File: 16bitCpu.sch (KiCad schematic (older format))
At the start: 0 parts

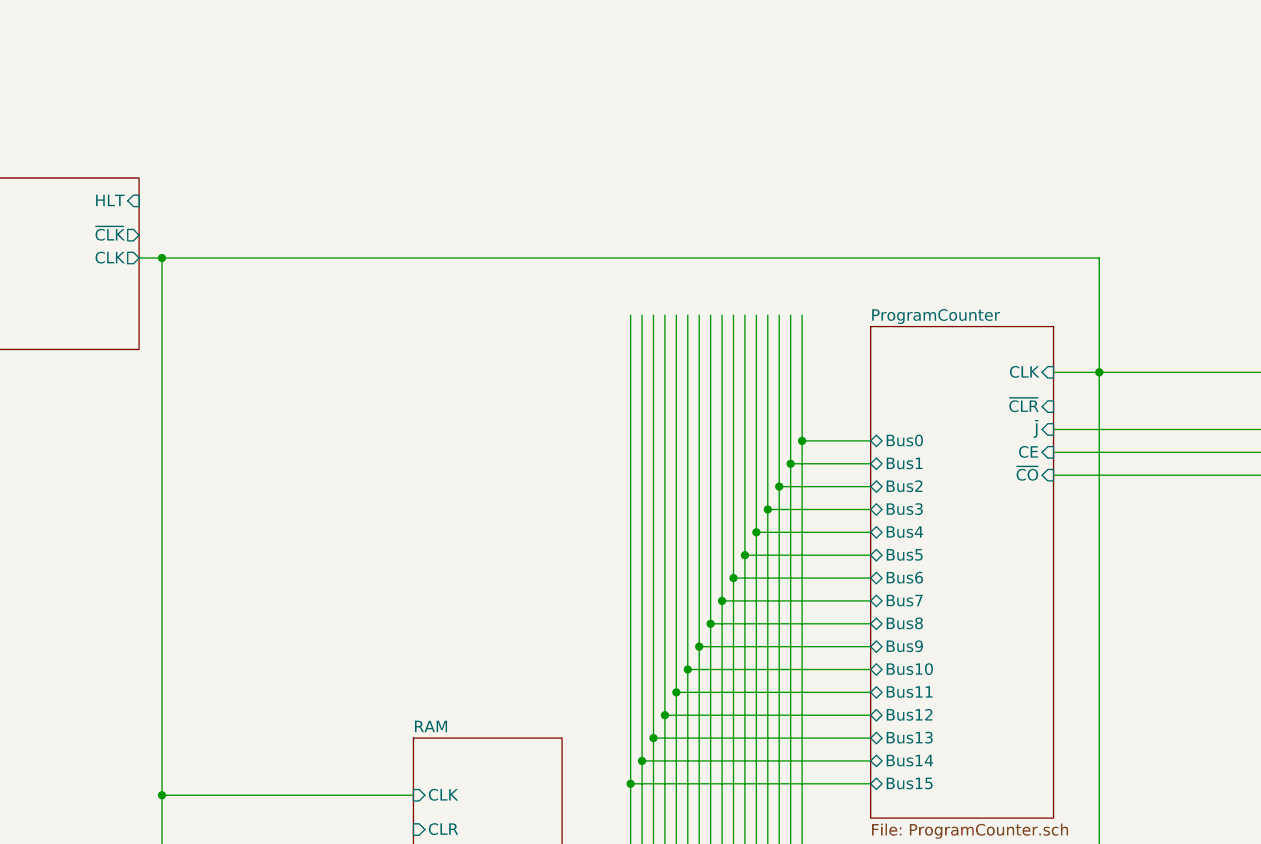
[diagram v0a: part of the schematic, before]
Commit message: changed ir to only hold 12
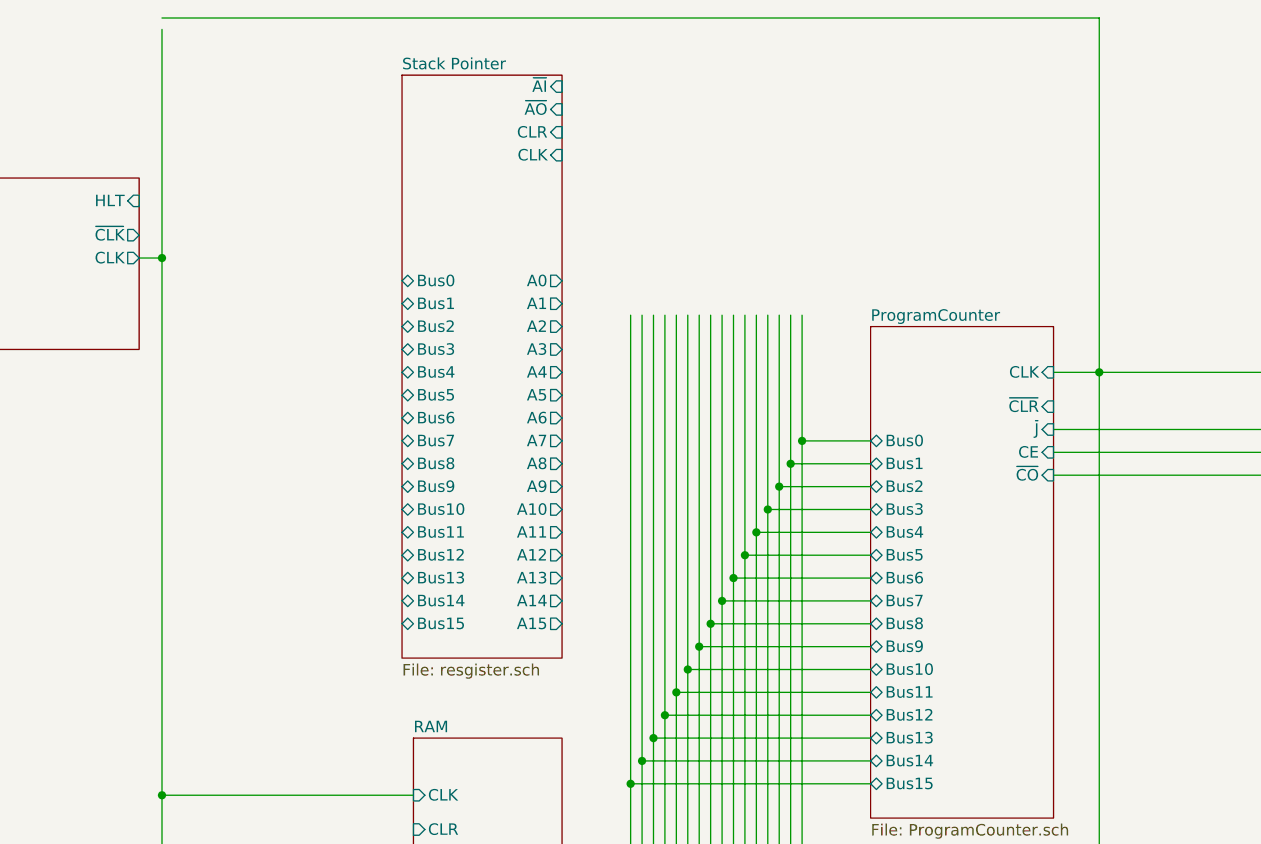
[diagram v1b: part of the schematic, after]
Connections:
- wire segments 411 -> 412
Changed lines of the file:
@@
 	7200 2100 7400 2100
-Wire Wire Line
-	7400 2100 7400 1600
 Wire Wire Line
 	5000 7250 6100 7250
@@
 F23 "~MEMWE" I L 4400 4850 50
 $EndSheet
-Connection ~ 3300 1600
 $Sheet
 S 4350 7100 650  1900
@@
 Connection ~ 7400 2100
 Wire Wire Line
-	3300 1600 7400 1600
+	3300 550  7400 550
 Wire Wire Line
 	7100 7800 7200 7800
@@
 Wire Wire Line
 	2650 7450 2650 13800
+$Sheet
+S 4350 800  700  2550
+U 5FB94562
+F0 "Stack Pointer" 50
+F1 "resgister.sch" 50
+F2 "CLK" I R 5050 1150 50
+F3 "Bus0" T L 4350 1700 50
+F4 "CLR" I R 5050 1050 50
+F5 "Bus1" T L 4350 1800 50
+F6 "Bus2" T L 4350 1900 50
+F7 "Bus3" T L 4350 2000 50
+F8 "Bus4" T L 4350 2100 50
+F9 "Bus5" T L 4350 2200 50
+F10 "Bus6" T L 4350 2300 50
+F11 "Bus7" T L 4350 2400 50
+F12 "Bus8" T L 4350 2500 50
+F13 "Bus9" T L 4350 2600 50
+F14 "Bus10" T L 4350 2700 50
+F15 "Bus11" T L 4350 2800 50
+F16 "Bus12" T L 4350 2900 50
+F17 "Bus13" T L 4350 3000 50
+F18 "Bus14" T L 4350 3100 50
+F19 "Bus15" T L 4350 3200 50
+F20 "A0" O R 5050 1700 50
+F21 "A1" O R 5050 1800 50
+F22 "A2" O R 5050 1900 50
+F23 "A3" O R 5050 2000 50
+F24 "A4" O R 5050 2100 50
+F25 "A5" O R 5050 2200 50
+F26 "A6" O R 5050 2300 50
+F27 "A7" O R 5050 2400 50
+F28 "A8" O R 5050 2500 50
+F29 "A9" O R 5050 2600 50
+F30 "A10" O R 5050 2700 50
+F31 "A11" O R 5050 2800 50
+F32 "A12" O R 5050 2900 50
+F33 "A13" O R 5050 3000 50
+F34 "A14" O R 5050 3100 50
+F35 "A15" O R 5050 3200 50
+F36 "~AO" I R 5050 950 50
+F37 "~AI" I R 5050 850 50
+$EndSheet
+Wire Wire Line
+	7400 550  7400 2100
+Wire Wire Line
+	3300 600  3300 1600
+Connection ~ 3300 1600
 $EndSCHEMATC

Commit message: non floating ram and ir , added stack register
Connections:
- wire segments 412 -> 452
- no-connect marks 0 -> 31
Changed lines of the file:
@@
 $Descr A3 11693 16535 portrait
 encoding utf-8
-Sheet 1 9
+Sheet 1 10
 Title ""
 Date ""
@@
 $EndDescr
 Wire Wire Line
-	5400 1850 5400 3800
-Wire Wire Line
-	5500 1850 5500 3600
-Wire Wire Line
-	5550 1850 5550 3500
-Wire Wire Line
-	5600 1850 5600 3400
-Wire Wire Line
-	5650 1850 5650 3300
-Wire Wire Line
-	5700 1850 5700 3200
-Wire Wire Line
-	5750 1850 5750 3100
-Wire Wire Line
-	5850 1850 5850 2900
-Wire Wire Line
-	5900 1850 5900 2800
-Wire Wire Line
-	5950 1850 5950 2700
-Wire Wire Line
-	6000 1850 6000 2600
-Wire Wire Line
-	6050 1850 6050 2500
+	5400 1850 5400 3200
+Wire Wire Line
+	5500 1850 5500 3000
+Wire Wire Line
+	5550 1850 5550 2900
+Wire Wire Line
+	5600 1850 5600 2800
+Wire Wire Line
+	5650 1850 5650 2700
+Wire Wire Line
+	5700 1850 5700 2600
+Wire Wire Line
+	5750 1850 5750 2500
+Wire Wire Line
+	5850 1850 5850 2300
+Wire Wire Line
+	5900 1850 5900 2200
+Wire Wire Line
+	5950 1850 5950 2100
+Wire Wire Line
+	6000 1850 6000 2000
+Wire Wire Line
+	6050 1850 6050 1900
 Wire Wire Line
 	6100 5550 6400 5550
@@
 F4 "CLK" O R 3200 1600 50
 $EndSheet
-Wire Wire Line
-	6100 1850 6100 2400
 Connection ~ 6100 4300
 Wire Wire Line
@@
 Connection ~ 5850 4800
 Wire Wire Line
-	5800 1850 5800 3000
+	5800 1850 5800 2400
 Connection ~ 5800 4900
 Wire Wire Line
@@
 	5050 5600 5450 5600
 Wire Wire Line
-	5450 1850 5450 3700
+	5450 1850 5450 3100
 Connection ~ 5450 5600
 Wire Wire Line
@@
 Connection ~ 5350 3900
 Wire Wire Line
-	5350 3900 5350 1850
+	5350 3900 5350 3300
 Wire Wire Line
 	7200 2100 7400 2100
@@
 F30 "CLR" O R 5150 13850 50
 F31 "~CLR" O R 5150 14000 50
+F32 "~SI" O L 4350 13950 50
+F33 "~SO" O L 4350 14050 50
 $EndSheet
 Wire Wire Line
@@
 Wire Wire Line
 	2650 7450 2650 13800
+Wire Wire Line
+	7400 550  7400 2100
+Wire Wire Line
+	3300 600  3300 1600
+Connection ~ 3300 1600
 $Sheet
-S 4350 800  700  2550
+S 4184 1300 816  2200
 U 5FB94562
 F0 "Stack Pointer" 50
-F1 "resgister.sch" 50
-F2 "CLK" I R 5050 1150 50
-F3 "Bus0" T L 4350 1700 50
-F4 "CLR" I R 5050 1050 50
-F5 "Bus1" T L 4350 1800 50
-F6 "Bus2" T L 4350 1900 50
-F7 "Bus3" T L 4350 2000 50
-F8 "Bus4" T L 4350 2100 50
-F9 "Bus5" T L 4350 2200 50
-F10 "Bus6" T L 4350 2300 50
-F11 "Bus7" T L 4350 2400 50
-F12 "Bus8" T L 4350 2500 50
-F13 "Bus9" T L 4350 2600 50
-F14 "Bus10" T L 4350 2700 50
-F15 "Bus11" T L 4350 2800 50
-F16 "Bus12" T L 4350 2900 50
-F17 "Bus13" T L 4350 3000 50
-F18 "Bus14" T L 4350 3100 50
-F19 "Bus15" T L 4350 3200 50
-F20 "A0" O R 5050 1700 50
-F21 "A1" O R 5050 1800 50
-F22 "A2" O R 5050 1900 50
-F23 "A3" O R 5050 2000 50
-F24 "A4" O R 5050 2100 50
-F25 "A5" O R 5050 2200 50
-F26 "A6" O R 5050 2300 50
-F27 "A7" O R 5050 2400 50
-F28 "A8" O R 5050 2500 50
-F29 "A9" O R 5050 2600 50
-F30 "A10" O R 5050 2700 50
-F31 "A11" O R 5050 2800 50
-F32 "A12" O R 5050 2900 50
-F33 "A13" O R 5050 3000 50
-F34 "A14" O R 5050 3100 50
-F35 "A15" O R 5050 3200 50
-F36 "~AO" I R 5050 950 50
-F37 "~AI" I R 5050 850 50
+F1 "stack.sch" 50
+F2 "CLK" I L 4184 1650 50
+F3 "Bus0" T R 5000 1800 50
+F4 "CLR" I L 4184 1550 50
+F5 "Bus1" T R 5000 1900 50
+F6 "Bus2" T R 5000 2000 50
+F7 "Bus3" T R 5000 2100 50
+F8 "Bus4" T R 5000 2200 50
+F9 "Bus5" T R 5000 2300 50
+F10 "Bus6" T R 5000 2400 50
+F11 "Bus7" T R 5000 2500 50
+F12 "Bus8" T R 5000 2600 50
+F13 "Bus9" T R 5000 2700 50
+F14 "Bus10" T R 5000 2800 50
+F15 "Bus11" T R 5000 2900 50
+F16 "Bus12" T R 5000 3000 50
+F17 "Bus13" T R 5000 3100 50
+F18 "Bus14" T R 5000 3200 50
+F19 "Bus15" T R 5000 3300 50
+F20 "~SI" I L 4184 2100 50
+F21 "~SO" I L 4184 2200 50
 $EndSheet
 Wire Wire Line
-	7400 550  7400 2100
-Wire Wire Line
-	3300 600  3300 1600
-Connection ~ 3300 1600
+	3300 1600 3800 1600
+Wire Wire Line
+	3800 1650 4200 1650
+Wire Wire Line
+	5000 1800 6100 1800
+Wire Wire Line
+	6100 1800 6100 2400
+Wire Wire Line
+	5000 1900 6050 1900
+Connection ~ 6050 1900
+Wire Wire Line
+	6050 1900 6050 2500
+Wire Wire Line
+	5000 2000 6000 2000
+Connection ~ 6000 2000
+Wire Wire Line
+	6000 2000 6000 2600
+Wire Wire Line
+	5000 2100 5950 2100
+Connection ~ 5950 2100
+Wire Wire Line
+	5950 2100 5950 2700
+Wire Wire Line
+	5000 2200 5900 2200
+Connection ~ 5900 2200
+Wire Wire Line
+	5900 2200 5900 2800
+Wire Wire Line
+	5000 2300 5850 2300
+Connection ~ 5850 2300
+Wire Wire Line
+	5850 2300 5850 2900
+Wire Wire Line
+	5000 2400 5800 2400
+Connection ~ 5800 2400
+Wire Wire Line
+	5800 2400 5800 3000
+Wire Wire Line
+	5000 2500 5750 2500
+Connection ~ 5750 2500
+Wire Wire Line
+	5750 2500 5750 3100
+Wire Wire Line
+	5000 2600 5700 2600
+Connection ~ 5700 2600
+Wire Wire Line
+	5700 2600 5700 3200
+Wire Wire Line
+	5000 2700 5650 2700
+Connection ~ 5650 2700
+Wire Wire Line
+	5650 2700 5650 3300
+Wire Wire Line
+	5000 2800 5600 2800
+Connection ~ 5600 2800
+Wire Wire Line
+	5600 2800 5600 3400
+Wire Wire Line
+	5000 2900 5550 2900
+Connection ~ 5550 2900
+Wire Wire Line
+	5550 2900 5550 3500
+Wire Wire Line
+	5000 3000 5500 3000
+Connection ~ 5500 3000
+Wire Wire Line
+	5500 3000 5500 3600
+Wire Wire Line
+	5000 3100 5450 3100
+Connection ~ 5450 3100
+Wire Wire Line
+	5450 3100 5450 3700
+Wire Wire Line
+	5000 3200 5400 3200
+Connection ~ 5400 3200
+Wire Wire Line
+	5400 3200 5400 3800
+Wire Wire Line
+	5000 3300 5350 3300
+Connection ~ 5350 3300
+Wire Wire Line
+	5350 3300 5350 1850
+NoConn ~ 6050 1850
+NoConn ~ 6000 1850
+NoConn ~ 5950 1850
+NoConn ~ 5900 1850
+NoConn ~ 5850 1850
+NoConn ~ 5800 1850
+NoConn ~ 5750 1850
+NoConn ~ 5700 1850
+NoConn ~ 5650 1850
+NoConn ~ 5600 1850
+NoConn ~ 5550 1850
+NoConn ~ 5500 1850
+NoConn ~ 5450 1850
+NoConn ~ 5400 1850
+NoConn ~ 5350 1850
+NoConn ~ 5350 15650
+NoConn ~ 5400 15650
+NoConn ~ 5450 15650
+NoConn ~ 5500 15650
+NoConn ~ 5550 15650
+NoConn ~ 5600 15650
+NoConn ~ 5650 15650
+NoConn ~ 5700 15650
+NoConn ~ 5750 15650
+NoConn ~ 5800 15650
+NoConn ~ 5850 15650
+NoConn ~ 5900 15650
+NoConn ~ 5950 15650
+NoConn ~ 6000 15650
+NoConn ~ 6050 15650
+NoConn ~ 6100 15650
+Wire Wire Line
+	4350 13950 1750 13950
+Wire Wire Line
+	1750 13950 1750 2100
+Wire Wire Line
+	1750 2100 4200 2100
+Wire Wire Line
+	4350 14050 1700 14050
+Wire Wire Line
+	1700 14050 1700 2200
+Wire Wire Line
+	1700 2200 4200 2200
+Wire Wire Line
+	3800 1600 3800 1650
 $EndSCHEMATC

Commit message: Added X register
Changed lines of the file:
@@
 $Descr A3 11693 16535 portrait
 encoding utf-8
-Sheet 1 10
+Sheet 1 11
 Title ""
 Date ""
@@
 F32 "~SI" O L 4350 13950 50
 F33 "~SO" O L 4350 14050 50
+F34 "~XI" O L 4350 12750 50
+F35 "~XO" O L 4350 12850 50
 $EndSheet
 Wire Wire Line
-	6100 11600 6100 15650
-Wire Wire Line
-	6050 11550 6050 15650
-Wire Wire Line
-	6000 11500 6000 15650
-Wire Wire Line
-	5950 11450 5950 15650
-Wire Wire Line
-	5900 11400 5900 15650
-Wire Wire Line
-	5850 11350 5850 15650
-Wire Wire Line
-	5800 11300 5800 15650
-Wire Wire Line
-	5750 11250 5750 15650
-Wire Wire Line
-	5700 11200 5700 15650
-Wire Wire Line
-	5650 11150 5650 15650
-Wire Wire Line
-	5600 11100 5600 15650
-Wire Wire Line
-	5550 11050 5550 15650
-Wire Wire Line
-	5500 11000 5500 15650
-Wire Wire Line
-	5450 10950 5450 15650
-Wire Wire Line
-	5400 10900 5400 15650
-Wire Wire Line
-	5350 10850 5350 15650
+	6050 11550 6050 14200
+Wire Wire Line
+	5950 11450 5950 14400
+Wire Wire Line
+	5850 11350 5850 14600
+Wire Wire Line
+	5750 11250 5750 14800
+Wire Wire Line
+	5700 11200 5700 14900
+Wire Wire Line
+	5600 11100 5600 15100
+Wire Wire Line
+	5550 11050 5550 15200
+Wire Wire Line
+	5500 11000 5500 15300
 Wire Wire Line
 	8900 5450 10550 5450
@@
 	3300 600  3300 1600
 Connection ~ 3300 1600
-$Sheet
-S 4184 1300 816  2200
-U 5FB94562
-F0 "Stack Pointer" 50
-F1 "stack.sch" 50
-F2 "CLK" I L 4184 1650 50
-F3 "Bus0" T R 5000 1800 50
-F4 "CLR" I L 4184 1550 50
-F5 "Bus1" T R 5000 1900 50
-F6 "Bus2" T R 5000 2000 50
-F7 "Bus3" T R 5000 2100 50
-F8 "Bus4" T R 5000 2200 50
-F9 "Bus5" T R 5000 2300 50
-F10 "Bus6" T R 5000 2400 50
-F11 "Bus7" T R 5000 2500 50
-F12 "Bus8" T R 5000 2600 50
-F13 "Bus9" T R 5000 2700 50
-F14 "Bus10" T R 5000 2800 50
-F15 "Bus11" T R 5000 2900 50
-F16 "Bus12" T R 5000 3000 50
-F17 "Bus13" T R 5000 3100 50
-F18 "Bus14" T R 5000 3200 50
-F19 "Bus15" T R 5000 3300 50
-F20 "~SI" I L 4184 2100 50
-F21 "~SO" I L 4184 2200 50
-$EndSheet
 Wire Wire Line
 	3300 1600 3800 1600
@@
 	3800 1650 4200 1650
 Wire Wire Line
-	5000 1800 6100 1800
-Wire Wire Line
 	6100 1800 6100 2400
-Wire Wire Line
-	5000 1900 6050 1900
 Connection ~ 6050 1900
 Wire Wire Line
 	6050 1900 6050 2500
-Wire Wire Line
-	5000 2000 6000 2000
 Connection ~ 6000 2000
 Wire Wire Line
 	6000 2000 6000 2600
-Wire Wire Line
-	5000 2100 5950 2100
 Connection ~ 5950 2100
 Wire Wire Line
 	5950 2100 5950 2700
-Wire Wire Line
-	5000 2200 5900 2200
 Connection ~ 5900 2200
 Wire Wire Line
 	5900 2200 5900 2800
-Wire Wire Line
-	5000 2300 5850 2300
 Connection ~ 5850 2300
 Wire Wire Line
 	5850 2300 5850 2900
-Wire Wire Line
-	5000 2400 5800 2400
 Connection ~ 5800 2400
 Wire Wire Line
 	5800 2400 5800 3000
-Wire Wire Line
-	5000 2500 5750 2500
 Connection ~ 5750 2500
 Wire Wire Line
 	5750 2500 5750 3100
-Wire Wire Line
-	5000 2600 5700 2600
 Connection ~ 5700 2600
 Wire Wire Line
 	5700 2600 5700 3200
-Wire Wire Line
-	5000 2700 5650 2700
 Connection ~ 5650 2700
 Wire Wire Line
 	5650 2700 5650 3300
-Wire Wire Line
-	5000 2800 5600 2800
 Connection ~ 5600 2800
 Wire Wire Line
 	5600 2800 5600 3400
-Wire Wire Line
-	5000 2900 5550 2900
 Connection ~ 5550 2900
 Wire Wire Line
 	5550 2900 5550 3500
-Wire Wire Line
-	5000 3000 5500 3000
 Connection ~ 5500 3000
 Wire Wire Line
 	5500 3000 5500 3600
-Wire Wire Line
-	5000 3100 5450 3100
 Connection ~ 5450 3100
 Wire Wire Line
 	5450 3100 5450 3700
-Wire Wire Line
-	5000 3200 5400 3200
 Connection ~ 5400 3200
 Wire Wire Line
 	5400 3200 5400 3800
-Wire Wire Line
-	5000 3300 5350 3300
 Connection ~ 5350 3300
 Wire Wire Line
@@
 Wire Wire Line
 	3800 1600 3800 1650
+$Sheet
+S 4200 1100 750  2400
+U 61968B9B
+F0 "Stack" 50
+F1 "stack.sch" 50
+F2 "CLK" I L 4200 1650 50
+F3 "Bus0" T R 4950 1800 50
+F4 "Bus1" T R 4950 1900 50
+F5 "Bus2" T R 4950 2000 50
+F6 "Bus4" T R 4950 2200 50
+F7 "Bus5" T R 4950 2300 50
+F8 "Bus6" T R 4950 2400 50
+F9 "Bus7" T R 4950 2500 50
+F10 "Bus8" T R 4950 2600 50
+F11 "Bus9" T R 4950 2700 50
+F12 "Bus10" T R 4950 2800 50
+F13 "Bus11" T R 4950 2900 50
+F14 "Bus12" T R 4950 3000 50
+F15 "Bus13" T R 4950 3100 50
+F16 "Bus14" T R 4950 3200 50
+F17 "CLR" I L 4200 1750 50
+F18 "Bus3" T R 4950 2100 50
+F19 "~SI" I L 4200 2100 50
+F20 "~SO" I L 4200 2200 50
+F21 "Bus15" T R 4950 3300 50
+$EndSheet
+Wire Wire Line
+	4950 1800 6100 1800
+Wire Wire Line
+	4950 3300 5350 3300
+Wire Wire Line
+	4950 3200 5400 3200
+Wire Wire Line
+	4950 3100 5450 3100
+Wire Wire Line
+	4950 3000 5500 3000
+Wire Wire Line
+	4950 2900 5550 2900
+Wire Wire Line
+	4950 2800 5600 2800
+Wire Wire Line
+	4950 2700 5650 2700
+Wire Wire Line
+	4950 2600 5700 2600
+Wire Wire Line
+	4950 2500 5750 2500
+Wire Wire Line
+	4950 2400 5800 2400
+Wire Wire Line
+	4950 2300 5850 2300
+Wire Wire Line
+	4950 2200 5900 2200
+Wire Wire Line
+	4950 2100 5950 2100
+Wire Wire Line
+	4950 2000 6000 2000
+Wire Wire Line
+	4950 1900 6050 1900
+$Sheet
+S 950  14050 800  1800
+U 61DF6CC7
+F0 "Sheet61DF6CC6" 50
+F1 "registerx.sch" 50
+F2 "CLK" I L 950 14150 50
+F3 "Bus0" T R 1750 14100 50
+F4 "Bus1" T R 1750 14200 50
+F5 "Bus2" T R 1750 14300 50
+F6 "Bus4" T R 1750 14500 50
+F7 "Bus5" T R 1750 14600 50
+F8 "Bus6" T R 1750 14700 50
+F9 "Bus7" T R 1750 14800 50
+F10 "Bus8" T R 1750 14900 50
+F11 "Bus9" T R 1750 15000 50
+F12 "Bus10" T R 1750 15100 50
+F13 "Bus11" T R 1750 15200 50
+F14 "Bus12" T R 1750 15300 50
+F15 "Bus13" T R 1750 15400 50
+F16 "Bus14" T R 1750 15500 50
+F17 "CLR" I L 950 14250 50
+F18 "Bus3" T R 1750 14400 50
+F19 "~XI" I L 950 14500 50
+F20 "~XO" I L 950 14600 50
+F21 "Bus15" T R 1750 15600 50
+$EndSheet
+Wire Wire Line
+	1750 15600 5350 15600
+Wire Wire Line
+	5350 10850 5350 15600
+Connection ~ 5350 15600
+Wire Wire Line
+	5350 15600 5350 15650
+Wire Wire Line
+	1750 15500 5400 15500
+Wire Wire Line
+	5400 10900 5400 15500
+Connection ~ 5400 15500
+Wire Wire Line
+	5400 15500 5400 15650
+Wire Wire Line
+	1750 15400 5450 15400
+Wire Wire Line
+	5450 10950 5450 15400
+Connection ~ 5450 15400
+Wire Wire Line
+	5450 15400 5450 15650
+Wire Wire Line
+	1750 15300 5500 15300
+Connection ~ 5500 15300
+Wire Wire Line
+	5500 15300 5500 15650
+Wire Wire Line
+	1750 15200 5550 15200
+Connection ~ 5550 15200
+Wire Wire Line
+	5550 15200 5550 15650
+Wire Wire Line
+	1750 15100 5600 15100
+Connection ~ 5600 15100
+Wire Wire Line
+	5600 15100 5600 15650
+Wire Wire Line
+	1750 15000 5650 15000
+Wire Wire Line
+	5650 11150 5650 15000
+Connection ~ 5650 15000
+Wire Wire Line
+	5650 15000 5650 15650
+Wire Wire Line
+	1750 14900 5700 14900
+Connection ~ 5700 14900
+Wire Wire Line
+	5700 14900 5700 15650
+Wire Wire Line
+	1750 14800 5750 14800
+Connection ~ 5750 14800
+Wire Wire Line
+	5750 14800 5750 15650
+Wire Wire Line
+	1750 14700 5800 14700
+Wire Wire Line
+	5800 11300 5800 14700
+Connection ~ 5800 14700
+Wire Wire Line
+	5800 14700 5800 15650
+Wire Wire Line
+	1750 14600 5850 14600
+Connection ~ 5850 14600
+Wire Wire Line
+	5850 14600 5850 15650
+Wire Wire Line
+	1750 14500 5900 14500
+Wire Wire Line
+	5900 11400 5900 14500
+Connection ~ 5900 14500
+Wire Wire Line
+	5900 14500 5900 15650
+Wire Wire Line
+	1750 14400 5950 14400
+Connection ~ 5950 14400
+Wire Wire Line
+	5950 14400 5950 15650
+Wire Wire Line
+	1750 14300 6000 14300
+Wire Wire Line
+	6000 11500 6000 14300
+Connection ~ 6000 14300
+Wire Wire Line
+	6000 14300 6000 15650
+Wire Wire Line
+	1750 14200 6050 14200
+Connection ~ 6050 14200
+Wire Wire Line
+	6050 14200 6050 15650
+Wire Wire Line
+	1750 14100 6100 14100
+Wire Wire Line
+	6100 11600 6100 14100
+Connection ~ 6100 14100
+Wire Wire Line
+	6100 14100 6100 15650
+Wire Wire Line
+	4350 12750 750  12750
+Wire Wire Line
+	750  12750 750  14500
+Wire Wire Line
+	750  14500 950  14500
+Wire Wire Line
+	4350 12850 700  12850
+Wire Wire Line
+	700  12850 700  14600
+Wire Wire Line
+	700  14600 950  14600
+Wire Wire Line
+	2850 12600 600  12600
+Wire Wire Line
+	600  12600 600  14150
+Wire Wire Line
+	600  14150 950  14150
+Connection ~ 2850 12600
 $EndSCHEMATC
